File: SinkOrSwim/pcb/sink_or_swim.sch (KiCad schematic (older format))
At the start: 10 parts

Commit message: update parts
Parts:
- removed Q?: MOSFET_N, symbol MOSFET_N
- removed U? (x2): LMV358, symbol LMV358
- added Q?: AOD476, symbol AOD476
- added U?: OPA2170AIDR, symbol OPA2170AIDR
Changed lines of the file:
@@
 LIBS:contrib
 LIBS:valves
+LIBS:alphaomega
+LIBS:sink_or_swim-cache
 EELAYER 25 0
 EELAYER END
@@
 $EndDescr
 $Comp
-L LMV358 U?
-U 1 1 54D177C5
-P 3600 2800
-F 0 "U?" H 3550 3000 60  0000 L CNN
-F 1 "LMV358" H 3550 2550 60  0000 L CNN
-F 2 "" H 3600 2800 60  0000 C CNN
-F 3 "" H 3600 2800 60  0000 C CNN
-	1    3600 2800
-	1    0    0    -1
-$EndComp
-$Comp
 L R R?
 U 1 1 54D178FE
@@
 $EndComp
 $Comp
-L MOSFET_N Q?
-U 1 1 54D179BB
-P 4950 2800
-F 0 "Q?" H 4960 2970 50  0000 R CNN
-F 1 "MOSFET_N" H 4900 2650 50  0000 R CNN
-F 2 "" H 4950 2800 60  0000 C CNN
-F 3 "" H 4950 2800 60  0000 C CNN
-	1    4950 2800
-	1    0    0    -1
-$EndComp
-$Comp
 L R R?
 U 1 1 54D17ABD
@@
 Wire Wire Line
 	5050 1800 5050 2600
+Connection ~ 3500 1800
+Connection ~ 5050 1800
+$Comp
+L GND #PWR?
+U 1 1 54D182F9
+P 4200 2400
+F 0 "#PWR?" H 4200 2150 60  0001 C CNN
+F 1 "GND" H 4200 2250 60  0000 C CNN
+F 2 "" H 4200 2400 60  0000 C CNN
+F 3 "" H 4200 2400 60  0000 C CNN
+	1    4200 2400
+	1    0    0    -1
+$EndComp
+$Comp
+L C C?
+U 1 1 54D1849A
+P 4750 2100
+F 0 "C?" H 4800 2200 50  0000 L CNN
+F 1 "C" H 4800 2000 50  0000 L CNN
+F 2 "" H 4788 1950 30  0000 C CNN
+F 3 "" H 4750 2100 60  0000 C CNN
+	1    4750 2100
+	1    0    0    -1
+$EndComp
+$Comp
+L C C?
+U 1 1 54D18527
+P 3650 2100
+F 0 "C?" H 3700 2200 50  0000 L CNN
+F 1 "C" H 3700 2000 50  0000 L CNN
+F 2 "" H 3688 1950 30  0000 C CNN
+F 3 "" H 3650 2100 60  0000 C CNN
+	1    3650 2100
+	1    0    0    -1
+$EndComp
+Connection ~ 4200 2300
+Wire Wire Line
+	4750 1900 4750 1800
+Connection ~ 4750 1800
+Wire Wire Line
+	3650 1900 3650 1800
+Connection ~ 3650 1800
+Wire Wire Line
+	3650 2300 4200 2300
+Wire Wire Line
+	4750 2300 4300 2300
+Wire Wire Line
+	4300 2300 4300 2200
+Wire Wire Line
+	4300 2200 4200 2200
+Connection ~ 4200 2200
+$Comp
+L POT RV?
+U 1 1 54D1876B
+P 1950 3300
+F 0 "RV?" H 1950 3200 50  0000 C CNN
+F 1 "POT" H 1950 3300 50  0000 C CNN
+F 2 "" H 1950 3300 60  0000 C CNN
+F 3 "" H 1950 3300 60  0000 C CNN
+	1    1950 3300
+	0    1    1    0
+$EndComp
+Wire Wire Line
+	2100 3300 2100 1800
+Connection ~ 2100 1800
+$Comp
+L CONN_01X02 P?
+U 1 1 54D1894C
+P 6350 1850
+F 0 "P?" H 6350 2000 50  0000 C CNN
+F 1 "CONN_01X02" V 6450 1850 50  0000 C CNN
+F 2 "" H 6350 1850 60  0000 C CNN
+F 3 "" H 6350 1850 60  0000 C CNN
+	1    6350 1850
+	1    0    0    -1
+$EndComp
+$Comp
+L GND #PWR?
+U 1 1 54D189E8
+P 5950 2050
+F 0 "#PWR?" H 5950 1800 60  0001 C CNN
+F 1 "GND" H 5950 1900 60  0000 C CNN
+F 2 "" H 5950 2050 60  0000 C CNN
+F 3 "" H 5950 2050 60  0000 C CNN
+	1    5950 2050
+	1    0    0    -1
+$EndComp
+Wire Wire Line
+	5950 2050 5950 1900
+Wire Wire Line
+	5950 1900 6150 1900
+$Comp
+L OPA2170AIDR U?
+U 1 1 54D2DD18
+P 3600 2800
+F 0 "U?" H 3550 3000 60  0000 L CNN
+F 1 "OPA2170AIDR" H 3550 2550 60  0000 L CNN
+F 2 "" H 3600 2800 60  0000 C CNN
+F 3 "" H 3600 2800 60  0000 C CNN
+	1    3600 2800
+	1    0    0    -1
+$EndComp
+$Comp
+L AOD476 Q?
+U 1 1 54D2E120
+P 4950 2800
+F 0 "Q?" H 4960 2970 50  0000 R CNN
+F 1 "AOD476" H 4900 2650 50  0000 R CNN
+F 2 "" H 4950 2800 60  0000 C CNN
+F 3 "" H 4950 2800 60  0000 C CNN
+	1    4950 2800
+	1    0    0    -1
+$EndComp
 $Comp
 L TC1016 U?
@@
 	-1   0    0    -1
 $EndComp
-Connection ~ 3500 1800
-Connection ~ 5050 1800
-$Comp
-L GND #PWR?
-U 1 1 54D182F9
-P 4200 2400
-F 0 "#PWR?" H 4200 2150 60  0001 C CNN
-F 1 "GND" H 4200 2250 60  0000 C CNN
-F 2 "" H 4200 2400 60  0000 C CNN
-F 3 "" H 4200 2400 60  0000 C CNN
-	1    4200 2400
-	1    0    0    -1
-$EndComp
-Wire Wire Line
-	4200 2100 4200 2400
-$Comp
-L C C?
-U 1 1 54D1849A
-P 4750 2100
-F 0 "C?" H 4800 2200 50  0000 L CNN
-F 1 "C" H 4800 2000 50  0000 L CNN
-F 2 "" H 4788 1950 30  0000 C CNN
-F 3 "" H 4750 2100 60  0000 C CNN
-	1    4750 2100
-	1    0    0    -1
-$EndComp
-$Comp
-L C C?
-U 1 1 54D18527
-P 3650 2100
-F 0 "C?" H 3700 2200 50  0000 L CNN
-F 1 "C" H 3700 2000 50  0000 L CNN
-F 2 "" H 3688 1950 30  0000 C CNN
-F 3 "" H 3650 2100 60  0000 C CNN
-	1    3650 2100
-	1    0    0    -1
-$EndComp
-Connection ~ 4200 2300
-Wire Wire Line
-	4750 1900 4750 1800
-Connection ~ 4750 1800
-Wire Wire Line
-	3650 1900 3650 1800
-Connection ~ 3650 1800
-Wire Wire Line
-	3650 2300 4200 2300
-Wire Wire Line
-	4750 2300 4300 2300
-Wire Wire Line
-	4300 2300 4300 2200
-Wire Wire Line
-	4300 2200 4200 2200
-Connection ~ 4200 2200
-$Comp
-L POT RV?
-U 1 1 54D1876B
-P 1950 3300
-F 0 "RV?" H 1950 3200 50  0000 C CNN
-F 1 "POT" H 1950 3300 50  0000 C CNN
-F 2 "" H 1950 3300 60  0000 C CNN
-F 3 "" H 1950 3300 60  0000 C CNN
-	1    1950 3300
-	0    1    1    0
-$EndComp
-Wire Wire Line
-	2100 3300 2100 1800
-Connection ~ 2100 1800
-Wire Wire Line
-	2100 1800 3800 1800
-$Comp
-L CONN_01X02 P?
-U 1 1 54D1894C
-P 6350 1850
-F 0 "P?" H 6350 2000 50  0000 C CNN
-F 1 "CONN_01X02" V 6450 1850 50  0000 C CNN
-F 2 "" H 6350 1850 60  0000 C CNN
-F 3 "" H 6350 1850 60  0000 C CNN
-	1    6350 1850
-	1    0    0    -1
-$EndComp
-Wire Wire Line
-	4600 1800 6150 1800
-$Comp
-L GND #PWR?
-U 1 1 54D189E8
-P 5950 2050
-F 0 "#PWR?" H 5950 1800 60  0001 C CNN
-F 1 "GND" H 5950 1900 60  0000 C CNN
-F 2 "" H 5950 2050 60  0000 C CNN
-F 3 "" H 5950 2050 60  0000 C CNN
-	1    5950 2050
-	1    0    0    -1
-$EndComp
-Wire Wire Line
-	5950 2050 5950 1900
-Wire Wire Line
-	5950 1900 6150 1900
-$Comp
-L LMV358 U?
-U 1 1 54D18B24
-P 6050 4050
-F 0 "U?" H 6000 4250 60  0000 L CNN
-F 1 "LMV358" H 6000 3800 60  0000 L CNN
-F 2 "" H 6050 4050 60  0000 C CNN
-F 3 "" H 6050 4050 60  0000 C CNN
-	1    6050 4050
-	1    0    0    -1
-$EndComp
+Wire Wire Line
+	2100 1800 3750 1800
+Wire Wire Line
+	4200 2150 4200 2400
+Wire Wire Line
+	6150 1800 4650 1800
 $EndSCHEMATC

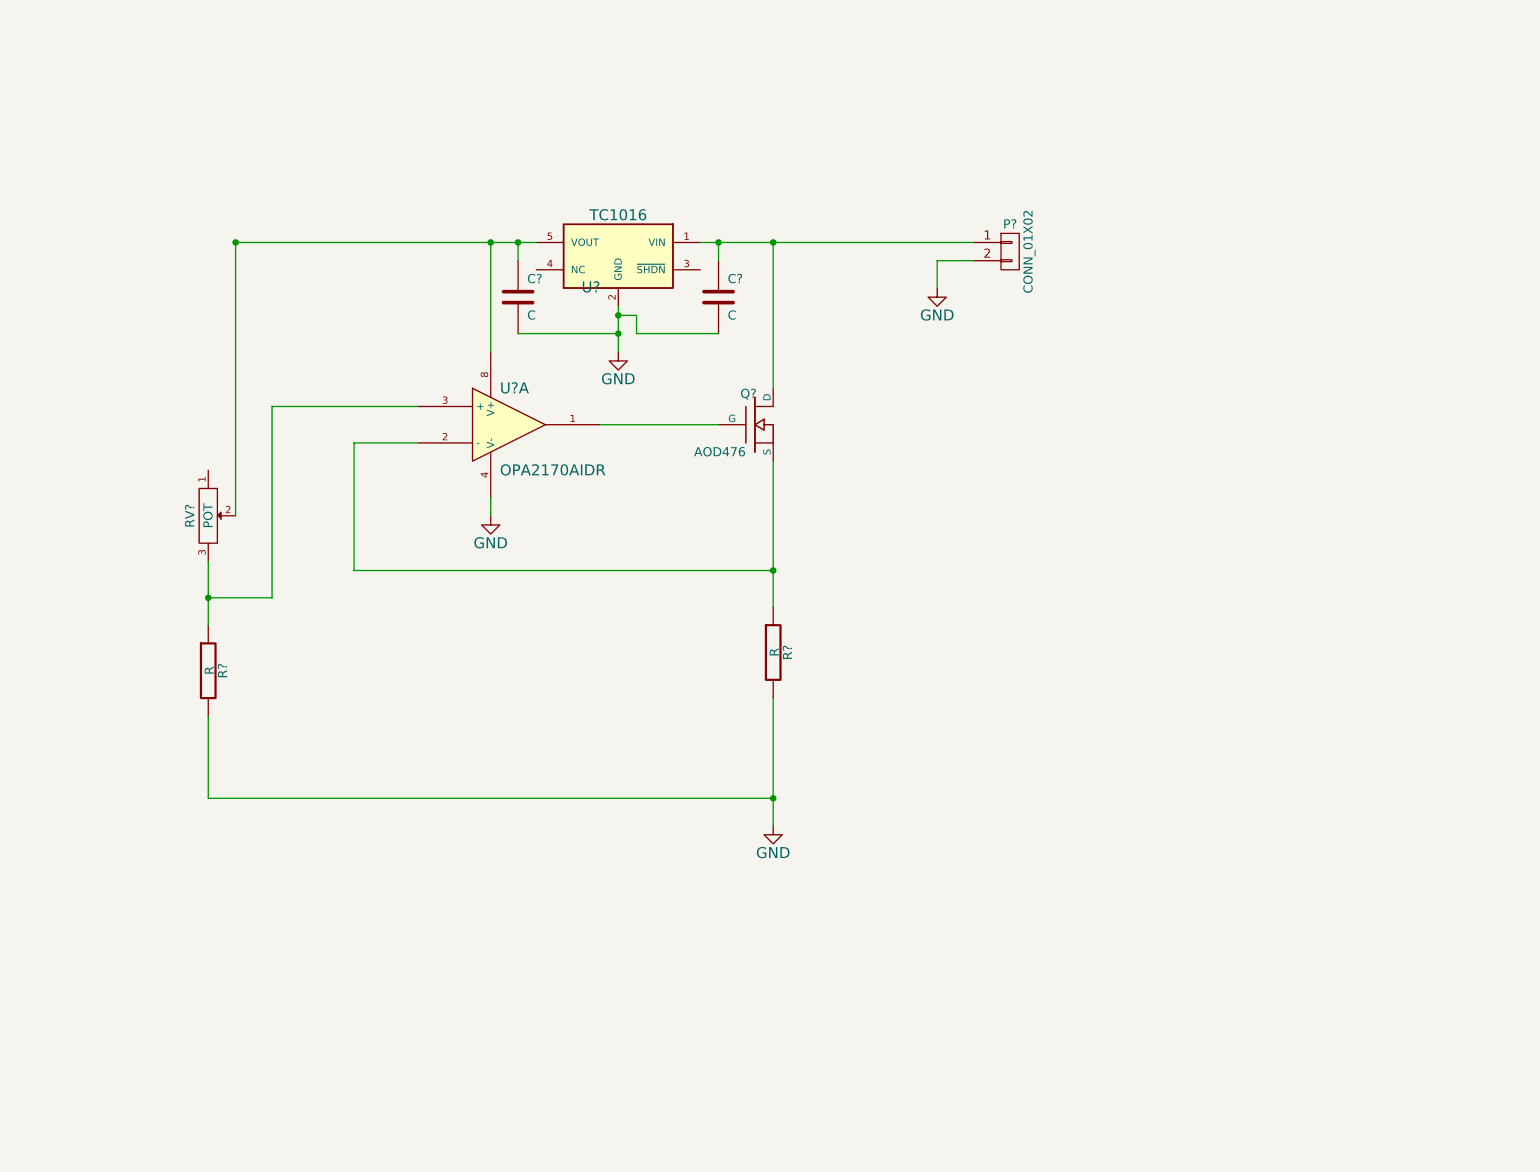
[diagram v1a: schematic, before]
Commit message: Fair number of parts are filled out now.  Schematic allows for separate power source.
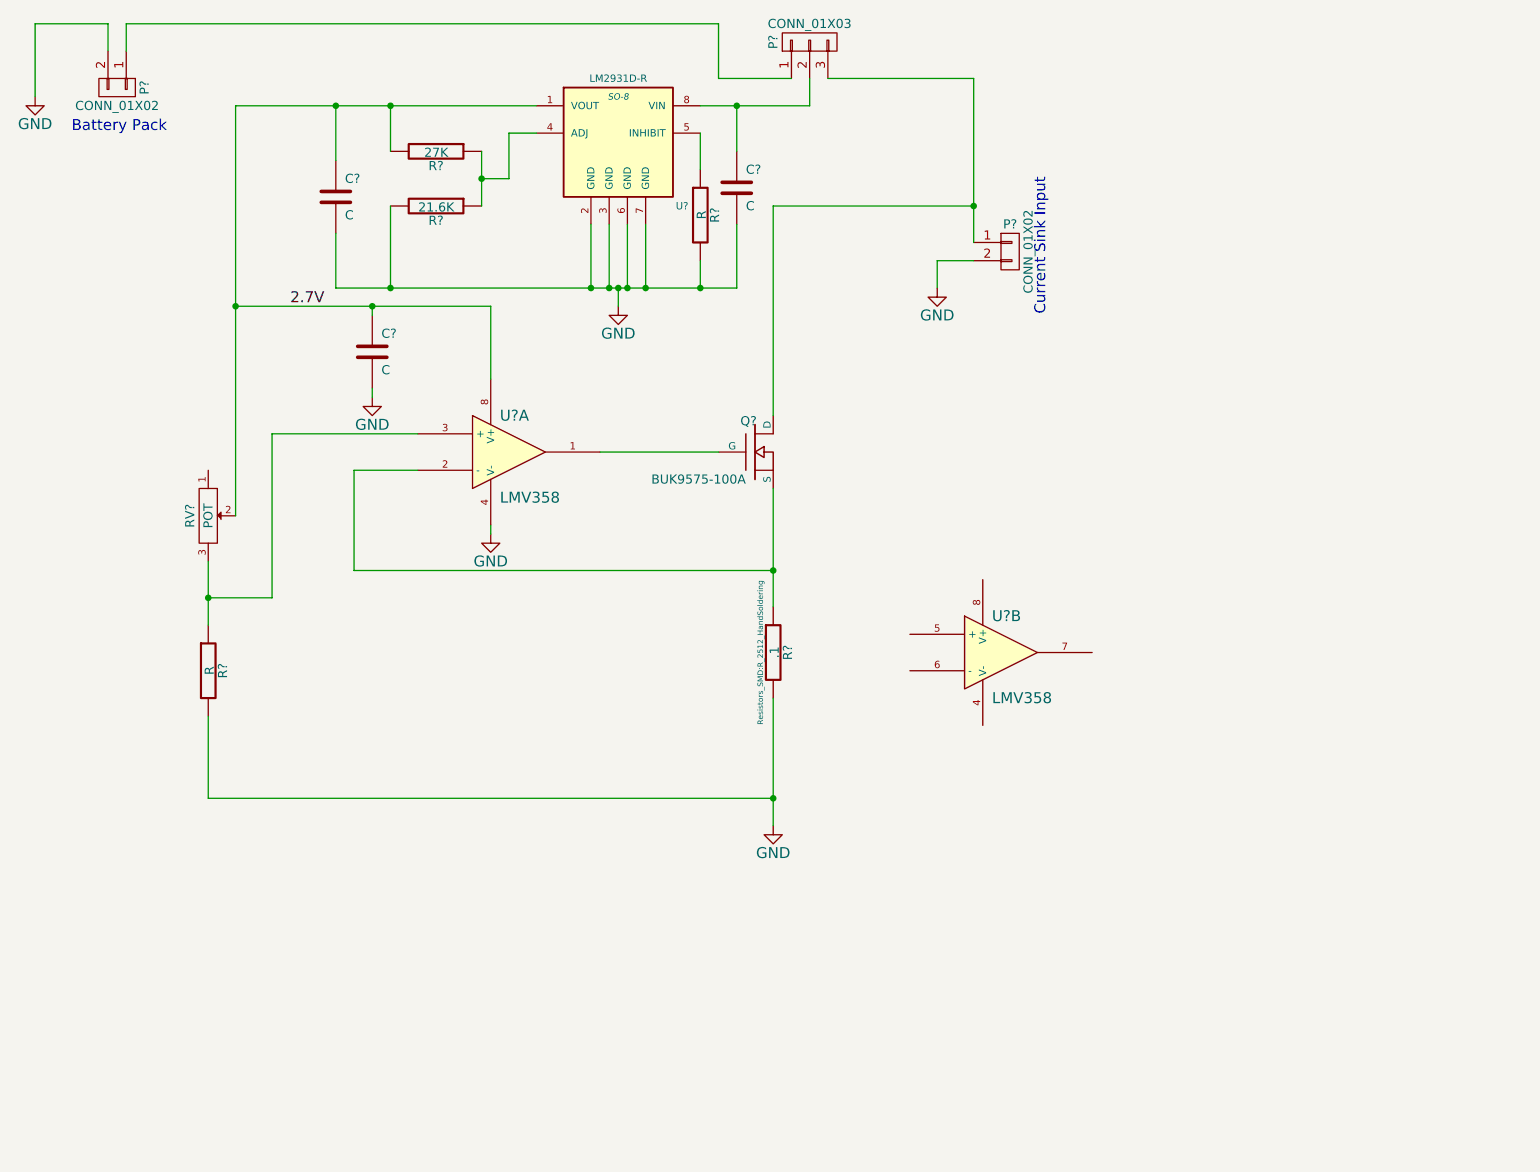
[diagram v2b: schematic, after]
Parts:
- removed Q?: AOD476, symbol AOD476
- removed U?: TC1016, symbol TC1016
- removed U?: OPA2170AIDR, symbol OPA2170AIDR
- added C?: C, symbol C
- added P?: CONN_01X03, symbol CONN_01X03
- added P?: CONN_01X02, symbol CONN_01X02
- added Q?: BUK9575-100A, symbol BUK9575-100A
- added R?: 27K, symbol R
- added R?: 21.6K, symbol R
- added R?: R, symbol R
- added U?: LM2931D-R, SO-8, symbol LM2931D-R
- added U? (x2): LMV358, symbol LMV358
- R?: value R -> .1; footprint (none) -> Resistors_SMD:R_2512_HandSoldering
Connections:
- net GND: now also C?.2, P?.2 (P2), R?.2, R?.2, U?.2 (GND), U?.3 (GND), U?.4 (V-), U?.6 (GND), U?.7 (GND)
- net at R?.1: now also Q?.S, U?.2 (-)
- net at R?.1, RV?.3: now also U?.3 (+)
- net at C?.1: now also P?.2 (P2), U?.8 (VIN); no longer P?.1 (P1)
- net 2.7V: now reaches C?.1, RV?.2
- net 2.7V: now also C?.1, R?.2, U?.1 (VOUT), U?.8 (V+)
- new net: P?.1 (P1), P?.3 (P3), Q?.D
- new net: R?.1, R?.1, U?.4 (ADJ)
- new net: R?.1, U?.5 (INHIBIT)
- new net: P?.1 (P1), P?.1 (P1)
- new net: Q?.G, U?.1
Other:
- note added: "Battery Pack"
- note added: "Current Sink Input"
- moved on the sheet: C?

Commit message: Added Hiearchical Sheets and Power Burn
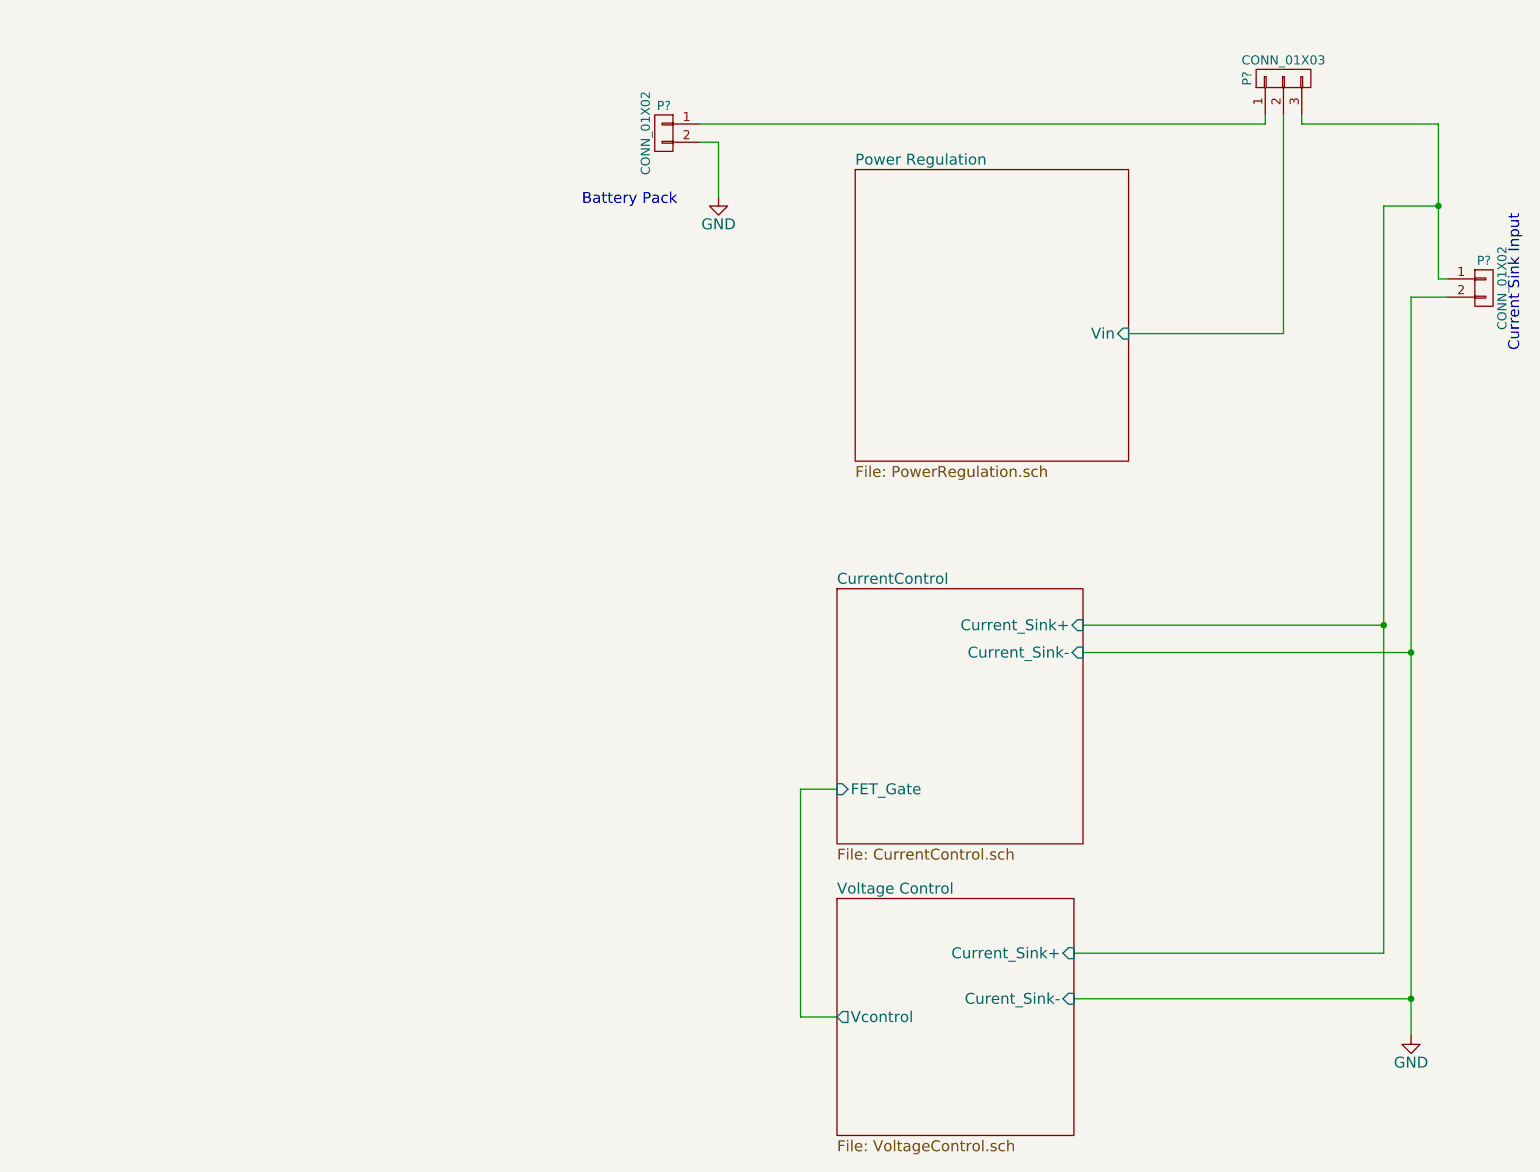
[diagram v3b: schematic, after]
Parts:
- removed C? (x3): C, symbol C
- removed Q?: BUK9575-100A, symbol BUK9575-100A
- removed R?: .1, Resistors_SMD:R_2512_HandSoldering, symbol R
- removed R? (x2): R, symbol R
- removed R?: 27K, symbol R
- removed R?: 21.6K, symbol R
- removed RV?: POT, symbol POT
- removed U?: LM2931D-R, SO-8, symbol LM2931D-R
- removed U? (x2): LMV358, symbol LMV358
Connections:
- net Power Regulation/Vin: now reaches P?.2 (P2)
- net CurrentControl/Current_Sink+: now reaches P?.1 (P1), P?.3 (P3)
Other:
- moved on the sheet: P?

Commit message: First annotation
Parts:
- gave numbers to parts that had none: 3
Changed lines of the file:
@@
 	8550 2100 8750 2100
 $Comp
-L CONN_01X03 P?
+L CONN_01X03 P102
 U 1 1 54DAD7C1
 P 7850 900
-F 0 "P?" H 7850 1100 50  0000 C CNN
+F 0 "P102" H 7850 1100 50  0000 C CNN
 F 1 "CONN_01X03" V 7950 900 50  0000 C CNN
 F 2 "" H 7850 900 60  0000 C CNN
@@
 	7850 1100 7850 2300
 $Comp
-L CONN_01X02 P?
+L CONN_01X02 P101
 U 1 1 54DADCB8
 P 4450 1200
-F 0 "P?" H 4450 1350 50  0000 C CNN
+F 0 "P101" H 4450 1350 50  0000 C CNN
 F 1 "CONN_01X02" V 4550 1200 50  0000 C CNN
 F 2 "" H 4450 1200 60  0000 C CNN
@@
 	4650 1150 7750 1150
 $Comp
-L GND #PWR?
+L GND #PWR101
 U 1 1 54DADF74
 P 4750 1550
-F 0 "#PWR?" H 4750 1300 60  0001 C CNN
+F 0 "#PWR101" H 4750 1300 60  0001 C CNN
 F 1 "GND" H 4750 1400 60  0000 C CNN
 F 2 "" H 4750 1550 60  0000 C CNN
@@
 F0 "CurrentControl" 60
 F1 "CurrentControl.sch" 60
-F3 "FET_Gate" I L 5400 4800 60
-F4 "Current_Sink+" I R 6750 3900 60
-F5 "Current_Sink-" I R 6750 4050 60
+F2 "FET_Gate" I L 5400 4800 60
+F3 "Current_Sink+" I R 6750 3900 60
+F4 "Current_Sink-" I R 6750 4050 60
 $EndSheet
 $Sheet
@@
 Connection ~ 8550 5950
 $Comp
-L GND #PWR?
+L GND #PWR102
 U 1 1 54DC7B33
 P 8550 6150
-F 0 "#PWR?" H 8550 5900 60  0001 C CNN
+F 0 "#PWR102" H 8550 5900 60  0001 C CNN
 F 1 "GND" H 8550 6000 60  0000 C CNN
 F 2 "" H 8550 6150 60  0000 C CNN
@@
 	7950 1150 8700 1150
 $Comp
-L CONN_01X02 P?
+L CONN_01X02 P103
 U 1 1 54D1894C
 P 8950 2050
-F 0 "P?" H 8950 2200 50  0000 C CNN
+F 0 "P103" H 8950 2200 50  0000 C CNN
 F 1 "CONN_01X02" V 9050 2050 50  0000 C CNN
 F 2 "" H 8950 2050 60  0000 C CNN

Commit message: Footprints associated and parts on pcb
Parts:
- P101, P103: footprint (none) -> Pin_Headers:Pin_Header_Straight_1x02
- P102: footprint (none) -> Pin_Headers:Pin_Header_Straight_1x03
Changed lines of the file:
@@
 F 0 "P102" H 7850 1100 50  0000 C CNN
 F 1 "CONN_01X03" V 7950 900 50  0000 C CNN
-F 2 "" H 7850 900 60  0000 C CNN
+F 2 "Pin_Headers:Pin_Header_Straight_1x03" H 7850 900 60  0001 C CNN
 F 3 "" H 7850 900 60  0000 C CNN
 	1    7850 900
@@
 F 0 "P101" H 4450 1350 50  0000 C CNN
 F 1 "CONN_01X02" V 4550 1200 50  0000 C CNN
-F 2 "" H 4450 1200 60  0000 C CNN
+F 2 "Pin_Headers:Pin_Header_Straight_1x02" H 4450 1200 60  0001 C CNN
 F 3 "" H 4450 1200 60  0000 C CNN
 	1    4450 1200
@@
 	4650 1150 7750 1150
 $Comp
-L GND #PWR101
+L GND #PWR01
 U 1 1 54DADF74
 P 4750 1550
-F 0 "#PWR101" H 4750 1300 60  0001 C CNN
+F 0 "#PWR01" H 4750 1300 60  0001 C CNN
 F 1 "GND" H 4750 1400 60  0000 C CNN
 F 2 "" H 4750 1550 60  0000 C CNN
@@
 Connection ~ 8550 5950
 $Comp
-L GND #PWR102
+L GND #PWR02
 U 1 1 54DC7B33
 P 8550 6150
-F 0 "#PWR102" H 8550 5900 60  0001 C CNN
+F 0 "#PWR02" H 8550 5900 60  0001 C CNN
 F 1 "GND" H 8550 6000 60  0000 C CNN
 F 2 "" H 8550 6150 60  0000 C CNN
@@
 F 0 "P103" H 8950 2200 50  0000 C CNN
 F 1 "CONN_01X02" V 9050 2050 50  0000 C CNN
-F 2 "" H 8950 2050 60  0000 C CNN
+F 2 "Pin_Headers:Pin_Header_Straight_1x02" H 8950 2050 60  0001 C CNN
 F 3 "" H 8950 2050 60  0000 C CNN
 	1    8950 2050
